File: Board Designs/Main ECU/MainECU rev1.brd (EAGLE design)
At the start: 121.2 x 79.8 mm, 145 parts, among them X1 CONNECTOR-37, X2 CONNECTOR-4AUTOSPORT, X3 CONNECTOR-4NANO-FIT-VERTICAL-4, X4 CONNECTOR-4NANO-FIT-VERTICAL-4

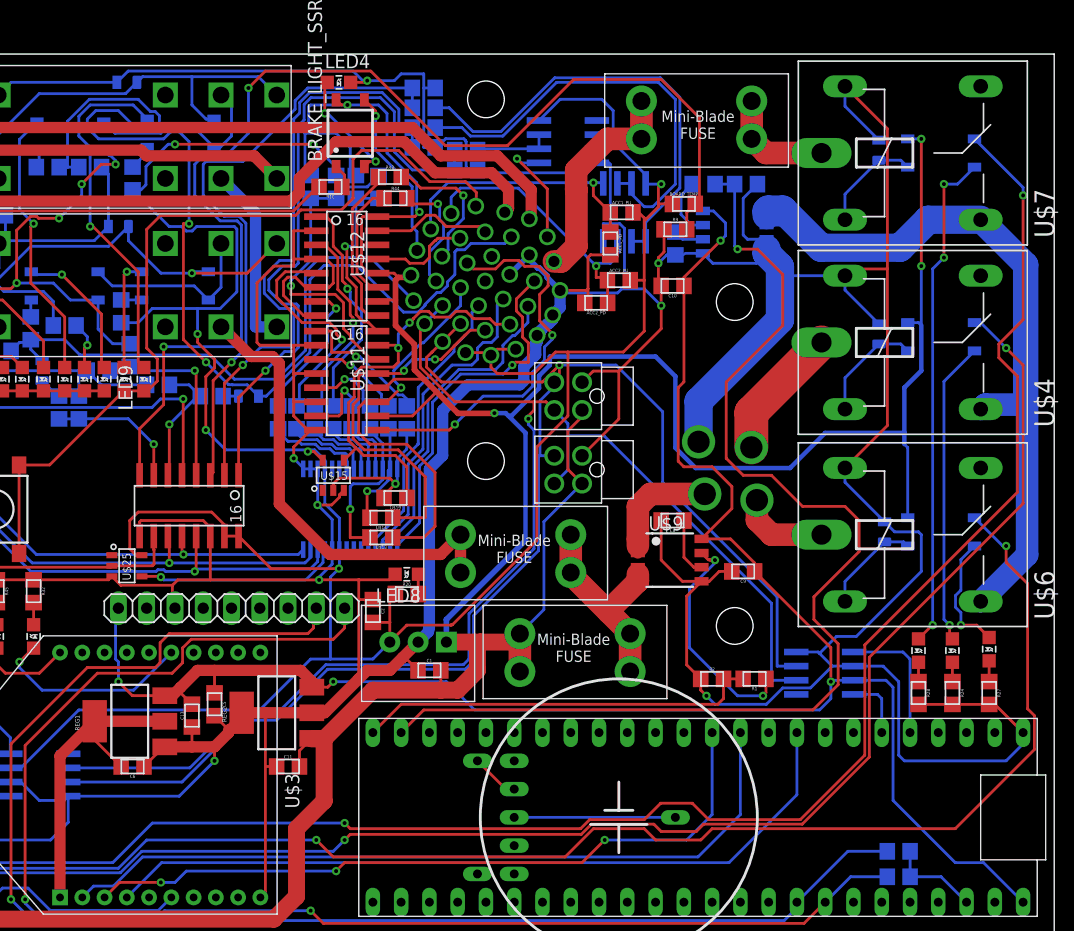
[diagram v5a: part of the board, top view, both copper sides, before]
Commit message: Main ECU rev{1,2}: Ensure no autosport intersecting, ensure connectors in same location on both revisions
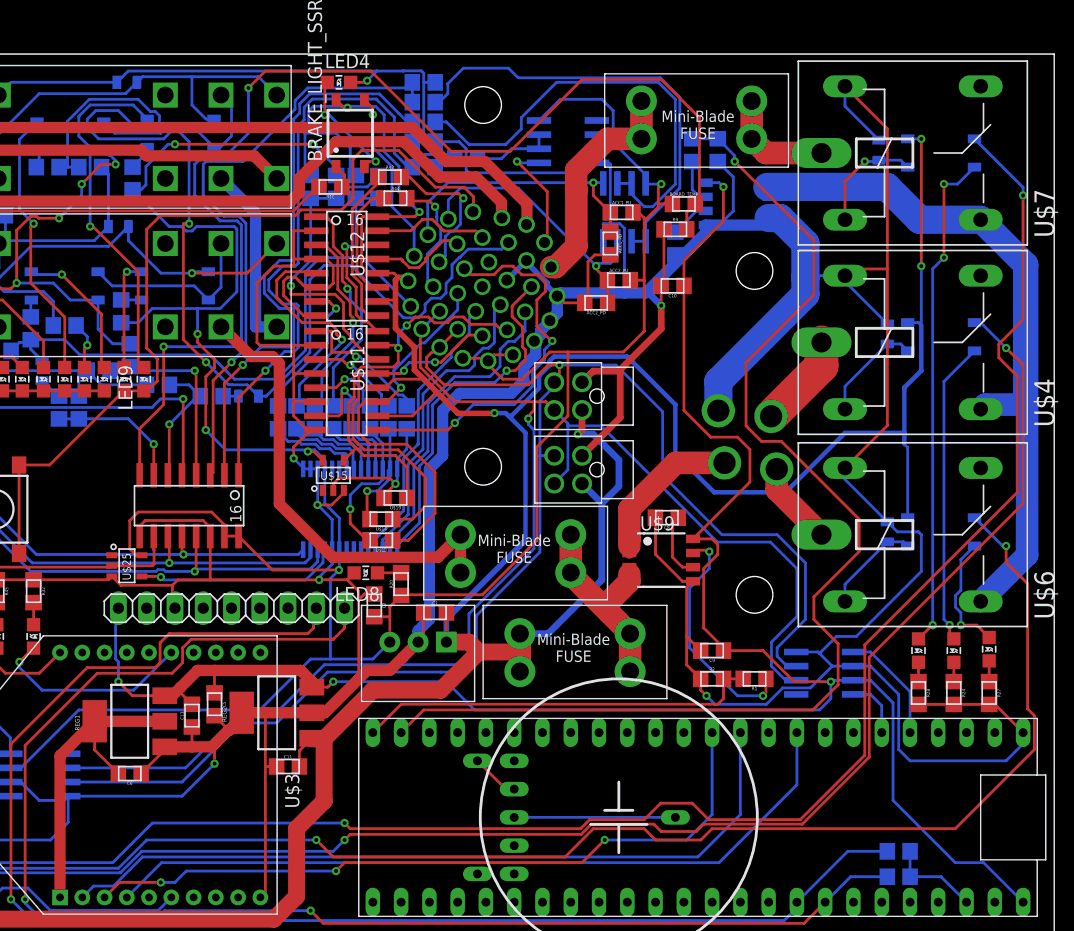
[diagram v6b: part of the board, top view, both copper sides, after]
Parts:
- moved C9 7.64 mm to (90.4, 26.2)
- moved C1 5.23 mm to (65.5, 29.6)
- moved R4 3.97 mm to (90.9, 71.1), turned to 90 degrees
- moved C12 3.82 mm to (64.5, 69.6)
- moved LED8 3.69 mm to (59.3, 33.1)
- moved X2 3.31 mm to (94.2, 45.7)
- moved R3 3.21 mm to (88.6, 71.1), turned to 90 degrees
- moved U$10 2.55 mm to (92.7, 66.3)
- moved R20 1.02 mm to (62.5, 32.1), turned to 90 degrees
- moved BR_FILTR 0.76 mm to (68.3, 70.4)
- moved D9 0.76 mm to (106.2, 54.6)
- moved U$9 0.76 mm to (85.9, 34.3)
- moved C6 0.68 mm to (38.1, 15.1)
- moved X1 0.57 mm to (69.8, 58.9)
- moved C8 0.57 mm to (86.4, 38.1)
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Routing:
- net TELEMETRY5V: track 168.3 -> 175.9 mm
- net +12V: track 430.9 -> 437.4 mm, vias 13 -> 14
- net GND: track 730.1 -> 735.5 mm, vias 11 -> 10
- net CANH: track 130.2 -> 134.2 mm
- net CANL: track 127.2 -> 131.0 mm
- net 12VIN: track 10.7 -> 14.2 mm
- net FAN2-: track 12.0 -> 8.51 mm
- net CURRENTSENSE2: track 67.1 -> 63.9 mm
- net +5V: track 292.5 -> 289.8 mm
- net COOLINGSENSE: track 104.0 -> 106.3 mm
- net READ_BRAKE: track 60.3 -> 58.5 mm
- net N$14: track 11.9 -> 10.2 mm
- net N$6: track 5.51 -> 4.00 mm
- net N$24: track 39.6 -> 41.1 mm
- net READ_ACCEL1: track 56.0 -> 54.8 mm
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
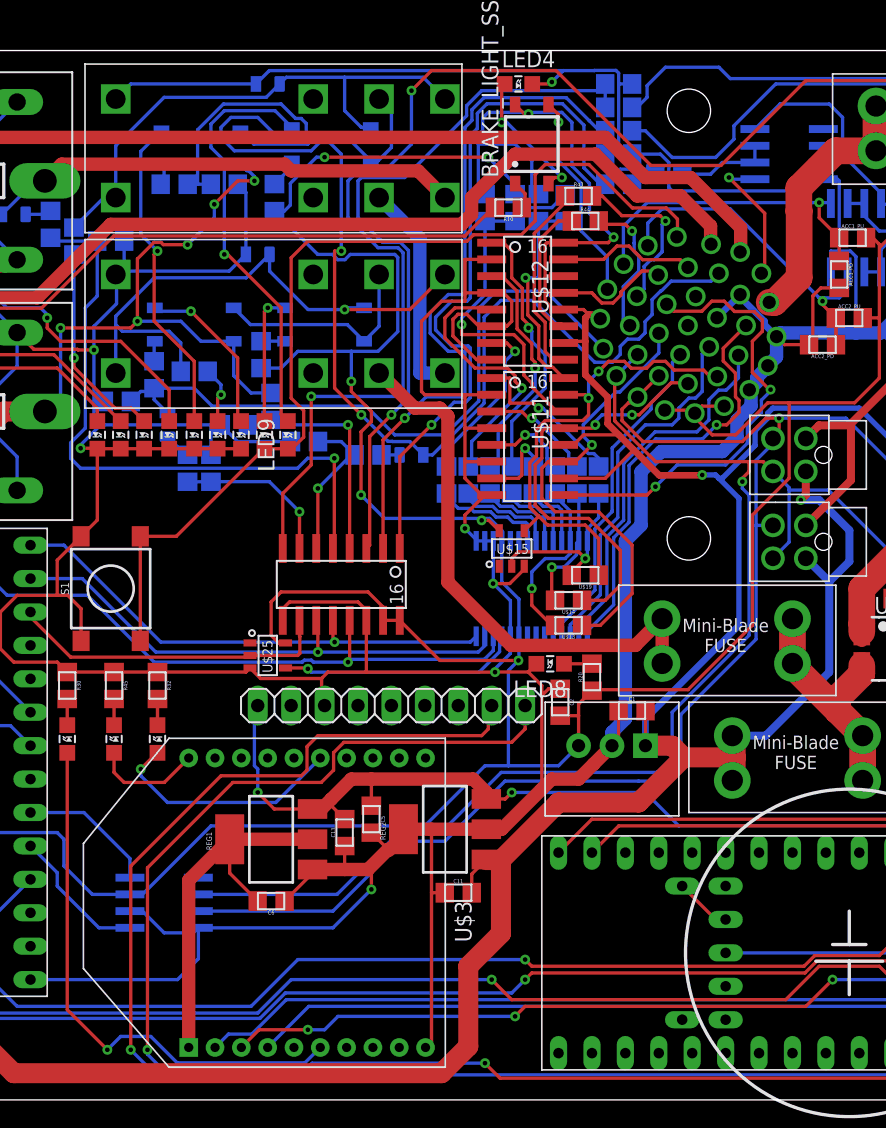
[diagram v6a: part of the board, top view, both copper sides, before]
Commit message: Main ECU rev1: Swap linear regulator with switching regulator
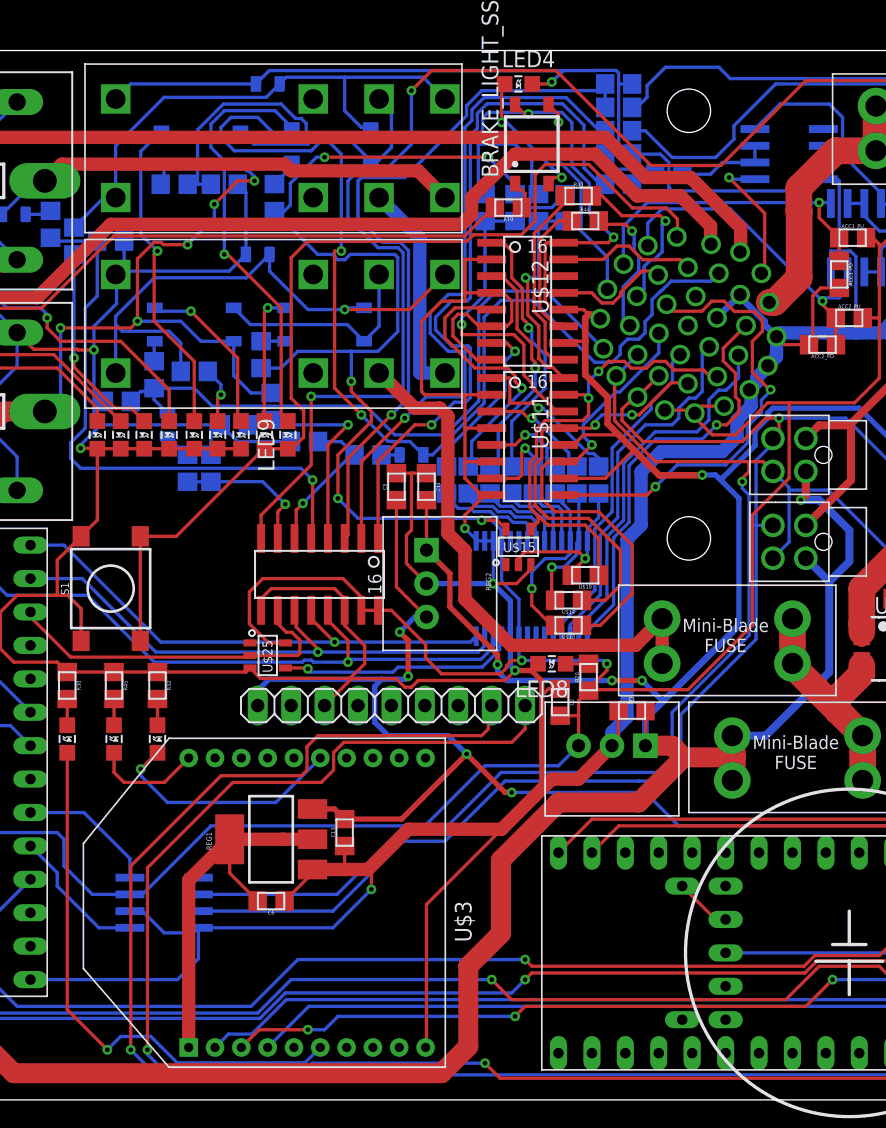
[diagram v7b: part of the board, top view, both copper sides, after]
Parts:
- REG2: device HyTechDevices:SOT223 -> HyTechDevices:OKI-78SR
- moved C11 31.0 mm to (49.9, 46.6), turned to 270 degrees
- moved C5 25.3 mm to (47.6, 46.6), turned to 90 degrees
- moved REG2 18.7 mm to (49.9, 39.2), turned to 270 degrees
- moved U$18 1.82 mm to (41.8, 39.9)
- moved U$15 0.52 mm to (56.9, 42.0)
- moved R20 0.25 mm to (62.2, 32.1)
- moved LED8 0.13 mm to (59.4, 33.1)
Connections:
- net GND: no longer REG2.4
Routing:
- net GND: track 735.5 -> 763.8 mm
- net TELEMETRY5V: track 175.9 -> 202.4 mm, vias 4 -> 6
- net +12V: track 437.4 -> 461.3 mm, vias 14 -> 17
- net +5V: track 289.8 -> 299.8 mm, vias 7 -> 8
- net SHUTDOWN_OUT_READ: track 48.6 -> 44.6 mm
- net CHIP_SELECT: track 24.8 -> 26.4 mm
- net MOSI_TEENSY: track 40.2 -> 41.7 mm
- net MISO_TEENSY: track 38.8 -> 40.3 mm
- net OKHS_READ: track 12.3 -> 11.0 mm
- net SCK_TEENSY: track 58.9 -> 60.1 mm
- net READ_BRAKE: track 58.5 -> 59.2 mm
- net DASH_CTRL8: track 13.7 -> 13.0 mm

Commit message: Main ECU rev{1-4}: Add warning about RTC cell assembly, specify current sensor input capacitor value, lower XBee LED resistor to 33R; Main ECU rev{2,4}: Specify MCP3208 input capacitor value; Main ECU rev4: Lower relay-controlling transistors' base resistor to 1k; Main ECU rev5: make all relevant changes previously listed
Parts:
- C10, C9: value (none) -> 0.1uF
- R45: value 2.3k -> 33
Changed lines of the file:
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@@
 <attribute name="VALUE" x="65.532" y="28.8798" size="0.3048" layer="27" align="top-center"/>
 </element>
-<element name="C10" library="HyTechDevices" package="0805" value="" x="86.868" y="58.928" smashed="yes" rot="R180">
+<element name="C10" library="HyTechDevices" package="0805" value="0.1uF" x="86.868" y="58.928" smashed="yes" rot="R180">
 <attribute name="NAME" x="86.868" y="58.2041" size="0.3048" layer="25" rot="R180" align="bottom-center"/>
 <attribute name="VALUE" x="86.868" y="59.6392" size="0.3048" layer="27" rot="R180" align="top-center"/>
@@
 <attribute name="VALUE" x="86.36" y="38.8112" size="0.3048" layer="27" rot="R180" align="top-center"/>
 </element>
-<element name="C9" library="HyTechDevices" package="0805" value="" x="90.424" y="26.162" smashed="yes" rot="R180">
+<element name="C9" library="HyTechDevices" package="0805" value="0.1uF" x="90.424" y="26.162" smashed="yes" rot="R180">
 <attribute name="NAME" x="90.424" y="25.4381" size="0.3048" layer="25" rot="R180" align="bottom-center"/>
 <attribute name="VALUE" x="90.424" y="26.8732" size="0.3048" layer="27" rot="R180" align="top-center"/>
@@
 <attribute name="VALUE" x="61.976" y="66.0908" size="0.3048" layer="27" align="top-center"/>
 </element>
-<element name="R45" library="HyTechDevices" package="0805" value="2.3k" x="26.162" y="31.496" smashed="yes" rot="R270">
+<element name="R45" library="HyTechDevices" package="0805" value="33" x="26.162" y="31.496" smashed="yes" rot="R270">
 <attribute name="NAME" x="26.8859" y="31.496" size="0.3048" layer="25" rot="R270" align="bottom-center"/>
 <attribute name="VALUE" x="25.4508" y="31.496" size="0.3048" layer="27" rot="R270" align="top-center"/>
